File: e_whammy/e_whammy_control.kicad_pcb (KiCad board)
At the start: 4 copper layers, 17 x 30 mm, 17 parts, among them J1 I/O connector, U1 HT7550-1, U2 DRV5056, U3 TLV6001UIDBVR

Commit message: First shot at layout
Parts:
- removed C2: 10uF, Capacitor_SMD:C_0805_2012Metric
- removed R4: 10K, Resistor_SMD:R_0402_1005Metric
- removed REF**: hole_1.7mm, cycfi_library:hole_1.7mm
- removed U1: HT7550-1, Package_TO_SOT_SMD:SOT-89-3
- added C3: 10uF, Capacitor_SMD:C_0603_1608Metric, F.Cu at (137.5, 145.4)
- added C4: 10uF, Capacitor_SMD:C_0603_1608Metric, F.Cu at (140.2, 148.0)
- added D2: 1N4148WS, Diode_SMD:D_SOD-323, F.Cu at (137.0, 148.0)
- added D3: 1N4148WS, Diode_SMD:D_SOD-323, F.Cu at (147.4, 150.7)
- added D4: 1N4148WS, Diode_SMD:D_SOD-323, F.Cu at (154.4, 150.7)
- added D5: 1N4148WS, Diode_SMD:D_SOD-323, F.Cu at (157.9, 150.7)
- added G***: LOGO, cycfi_library:infinity_logo_4mm, F.Cu at (161.7, 151.3)
- added J2: Conn_01x03, cycfi_library:pin_header_1x3p_2.54mm_smd_horizontal, B.Cu at (154.8, 148.5)
- added J3: Conn_01x02, Connector_PinHeader_2.54mm:PinHeader_1x02_P2.54mm_Vertical, F.Cu at (146.9, 141.1)
- added J4: Conn_01x02, Connector_PinHeader_2.54mm:PinHeader_1x02_P2.54mm_Vertical, F.Cu at (157.4, 141.1)
- added R10: 10K, Resistor_SMD:R_0402_1005Metric, F.Cu at (147.4, 148.8)
- added R11: 10K, Resistor_SMD:R_0402_1005Metric, F.Cu at (157.4, 148.7)
- added R12: 10K, Resistor_SMD:R_0402_1005Metric, F.Cu at (157.4, 145.4)
- added R13: 10K, Resistor_SMD:R_0402_1005Metric, F.Cu at (157.4, 144.3)
- added R14: 10K, Resistor_SMD:R_0402_1005Metric, F.Cu at (161.3, 143.2)
- added R15: 10K, Resistor_SMD:R_0402_1005Metric, F.Cu at (142.7, 150.7)
- added R16: 10K, Resistor_SMD:R_0402_1005Metric, F.Cu at (143.8, 150.7)
- added R8: 100K, Resistor_SMD:R_0402_1005Metric, F.Cu at (166.1, 143.2)
- added R9: 100K, Resistor_SMD:R_0402_1005Metric, F.Cu at (166.1, 149.5)
- added RV3: 10K, cycfi_library:TC33X-2, F.Cu at (166.7, 146.3)
- C1: value 10uF -> 100nF; footprint Capacitor_SMD:C_0805_2012Metric -> Capacitor_SMD:C_0402_1005Metric
- D1: value 1N4148W -> 1N4148WS; footprint Diode_SMD:D_SOD-123 -> Diode_SMD:D_SOD-323
- J1: value I/O connector -> Conn_01x03; footprint Connector_PinHeader_2.54mm:PinHeader_1x03_P2.54mm_Vertical -> cycfi_library:pin_header_1x3p_2.54mm_smd_horizontal; moved to B.Cu
- R2: value 4.7K -> 10K
- R6: value 100K -> 47K
- RV1: value 5K -> 10K
- U2: value DRV5056 -> HT7550-1
- U3: value TLV6001UIDBVR -> TLV9004IPWR; footprint Package_TO_SOT_SMD:SOT-23-5 -> cycfi_library:TSSOP-14_4.4x5mm_P0.65mm
- moved R7 59.5 mm to (157.4, 146.5), turned to 0 degrees
- moved R5 53.9 mm to (157.4, 147.6), turned to 180 degrees
- moved U3 52.4 mm to (152.4, 146.4), turned to 0 degrees
- moved J1 49.8 mm to (149.2, 143.5), turned to 180 degrees
- moved D1 49.5 mm to (150.8, 150.7), turned to 0 degrees
- moved R2 47.3 mm to (147.9, 144.7)
- moved C1 47.3 mm to (144.9, 150.7)
- moved RV2 47.1 mm to (161.8, 146.3), turned to 0 degrees
- moved R3 46.5 mm to (147.4, 147.7), turned to 0 degrees
- moved R1 45.2 mm to (146.8, 144.7)
- moved R6 44.0 mm to (147.4, 146.4)
- moved RV1 42.3 mm to (144.2, 146.3), turned to 0 degrees
- moved U2 40.2 mm to (140.2, 145.4), turned to 0 degrees
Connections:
- C1 pad 1: Net-(D1-K) -> /VREF
- D1 pad 2: V+ -> /PR
- J1 pad 1: OUT -> HE_SENSOR
- R1 pad 2: Net-(R1-Pad2) -> Net-(U3A--)
- R2 pad 1: Net-(R2-Pad1) -> Net-(U3A--)
- R2 pad 2: 5v -> /PRE
- R3 pad 1: Net-(U2-OUT) -> /PRE
- R3 pad 2: Net-(U3-+) -> Net-(D3-K)
- R5 pad 1: Net-(U3-+) -> /PRE
- R5 pad 2: 5v -> Net-(D5-A)
- R6 pad 1: Net-(U3--) -> Net-(R6-Pad1)
- R6 pad 2: Net-(R6-Pad2) -> HE_SENSOR
- R7 pad 1: Net-(R7-Pad1) -> /RO2
- RV1 pad 1: Net-(R2-Pad1) -> GND
- RV1 pad 2: Net-(R4-Pad1) -> Net-(R6-Pad1)
- RV1 pad 3: Net-(R1-Pad2) -> 5v
- RV2 pad 1: Net-(R6-Pad2) -> /RO1
- RV2 pad 2: Net-(R7-Pad1) -> /RO1
- RV2 pad 3: Net-(R7-Pad1) -> /RO2
- U2 pad 1: 5v -> GND
- U2 pad 2: Net-(U2-OUT) -> Net-(D2-K)
- U2 pad 3: GND -> 5v
- U3 pad 1: Net-(U3-+) -> /PRE
- U3 pad 2: GND -> Net-(U3A--)
- U3 pad 3: Net-(U3--) -> HE_SENSOR
- U3 pad 4: Net-(R7-Pad1) -> 5v
- U3 pad 5: 5v -> /DHI
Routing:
- net Net-(R7-Pad1): track 21.5 -> 0.00 mm, vias 2 -> 0
- net 5v: track 9.59 -> 0.00 mm, vias 6 -> 0
- net Net-(U3--): track 8.92 -> 0.00 mm, vias 2 -> 0
- net Net-(D1-K): track 6.79 -> 0.00 mm
- net Net-(R4-Pad1): track 6.50 -> 0.00 mm, vias 2 -> 0
- net V+: track 6.42 -> 0.00 mm
- net Net-(R6-Pad2): track 6.17 -> 0.00 mm
- net Net-(R1-Pad2): track 4.40 -> 0.00 mm
- net OUT: track 3.34 -> 0.00 mm
- net Net-(U3-+): track 3.33 -> 0.00 mm
- net Net-(U2-OUT): track 2.90 -> 0.00 mm
- net Net-(R2-Pad1): track 1.40 -> 0.00 mm
- removed copper zone on In1.Cu, net 5v
- removed copper zone on B.Cu, net GND
- removed copper zone on F.Cu, net GND
- removed copper zone on In2.Cu, net GND
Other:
- board size 17 x 30 mm -> 34 x 14 mm
- copper layers 4 -> 2
- board text added: "CENTER"
- board text added: "DBO"
- board text added: "DEADBAND"
- board text added: "HE v1.0"
- board text added: "HE-SENSOR"
- board text added: "OUTPUT"
- board text added: "RANGE"
- board text added: "RGO"
- board text removed: "GAIN"
- board text removed: "OFFS"

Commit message: E-Whammy layout complete (first shot)
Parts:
- moved D2 2.73 mm to (139.5, 149.1), turned to 0 degrees
- moved J1 2.54 mm to (149.2, 146.0)
- moved J2 2.54 mm to (154.8, 146.0)
- moved U2 2.40 mm to (140.3, 143.1)
- moved C4 1.58 mm to (140.3, 146.4), turned to -90 degrees
- moved C3 1.51 mm to (138.7, 146.4), turned to -90 degrees
- moved R6 0.27 mm to (147.3, 146.2)
- moved R12 0.25 mm to (157.4, 145.2)
- moved R11 0.20 mm to (157.4, 148.9)
- moved R13 0.20 mm to (157.4, 144.1)
- moved R10 0.16 mm to (147.4, 149.0)
- moved R3 0.16 mm to (147.4, 147.9)
- moved RV1 0.14 mm to (144.1, 146.3)
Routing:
- net 5v: track 0.00 -> 44.8 mm, vias 0 -> 2
- net /DHI: track 0.00 -> 37.9 mm
- net /DLO: track 0.00 -> 32.8 mm
- net /PRE: track 0.00 -> 30.3 mm, vias 0 -> 3
- net V+: track 0.00 -> 20.6 mm, vias 0 -> 1
- net /VREF: track 0.00 -> 20.1 mm, vias 0 -> 2
- net /PR: track 0.00 -> 20.1 mm, vias 0 -> 2
- net /RO2: track 0.00 -> 19.4 mm
- net /NR: track 0.00 -> 13.9 mm, vias 0 -> 2
- net /RO1: track 0.00 -> 10.6 mm
- net GND: track 0.00 -> 9.81 mm, vias 0 -> 7
- net Net-(U3D--): track 0.00 -> 8.29 mm, vias 0 -> 2
- net Net-(D5-A): track 0.00 -> 7.05 mm
- net HE_SENSOR: track 0.00 -> 6.33 mm, vias 0 -> 1
- net Net-(D2-K): track 0.00 -> 5.98 mm
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- added copper zone on B.Cu, net GND
- added copper zone on F.Cu, net GND

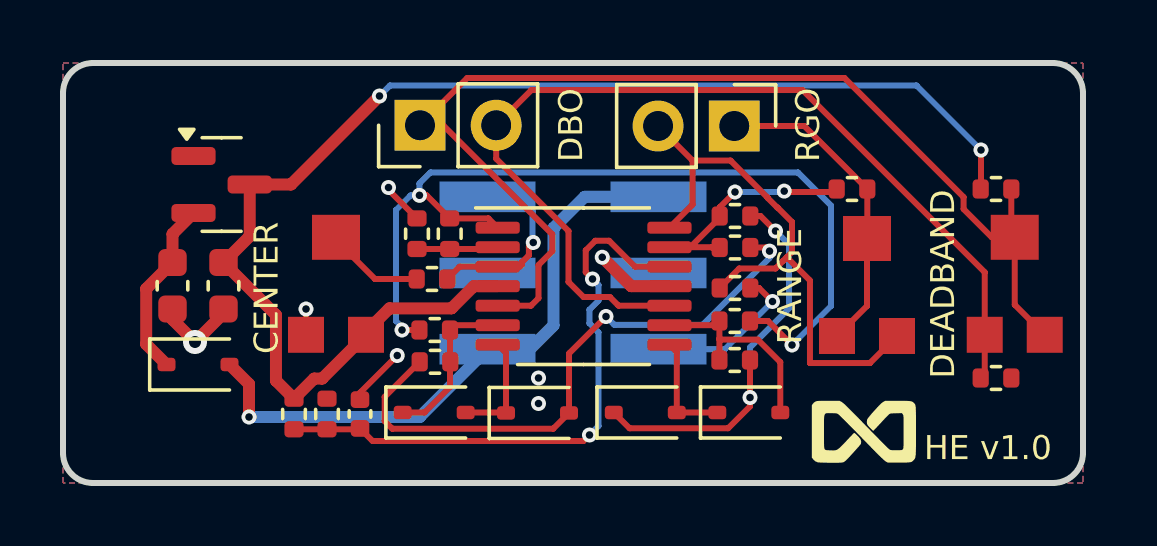
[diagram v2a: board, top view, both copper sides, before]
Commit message: E-Whammy layout looking good!
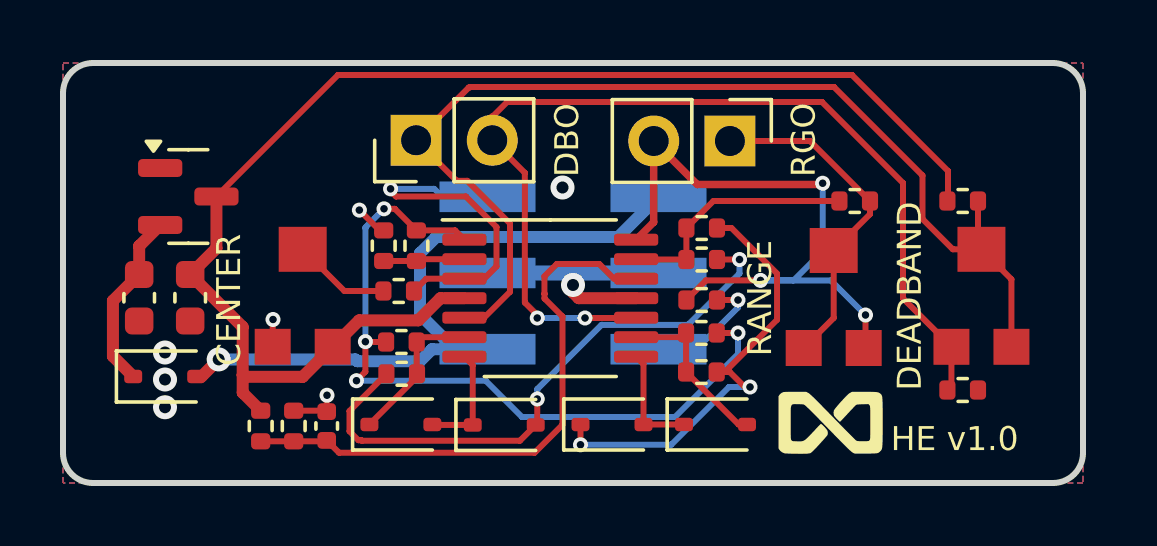
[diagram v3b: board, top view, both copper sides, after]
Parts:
- moved C1 1.18 mm to (143.8, 151.1)
- moved D3 1.18 mm to (146.3, 151.1)
- moved D5 1.18 mm to (156.8, 151.1)
- moved R1 1.18 mm to (145.7, 145.1)
- moved R10 1.18 mm to (146.3, 149.4)
- moved R12 1.18 mm to (156.3, 145.6)
- moved R13 1.18 mm to (156.3, 144.5)
- moved R16 1.18 mm to (142.7, 151.1)
- moved R6 1.18 mm to (146.2, 146.6)
- moved R7 1.18 mm to (156.3, 146.9)
- moved C3 1.18 mm to (137.5, 146.8)
- moved D2 1.18 mm to (138.4, 149.4)
- moved RV2 1.18 mm to (160.7, 146.7)
- moved D1 1.18 mm to (149.7, 151.1)
- moved D4 1.18 mm to (153.3, 151.1)
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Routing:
- net HE_SENSOR: track 6.33 -> 11.9 mm
- net /PRE: track 30.3 -> 25.4 mm, vias 3 -> 4
- net V+: track 20.6 -> 23.6 mm
- net /RO2: track 19.4 -> 22.4 mm, vias 0 -> 3
- net GND: track 9.81 -> 11.8 mm, vias 7 -> 8
- net /DHI: track 37.9 -> 36.4 mm
- net /NR: track 13.9 -> 15.3 mm
- net Net-(D5-A): track 7.05 -> 5.78 mm
- net /VREF: track 20.1 -> 19.3 mm, vias 2 -> 0
- net /RO1: track 10.6 -> 11.3 mm
- net 5v: track 44.8 -> 45.4 mm, vias 2 -> 0
- net /DLO: track 32.8 -> 33.3 mm, vias 0 -> 2
- net Net-(U3D--): track 8.29 -> 8.20 mm, vias 2 -> 0

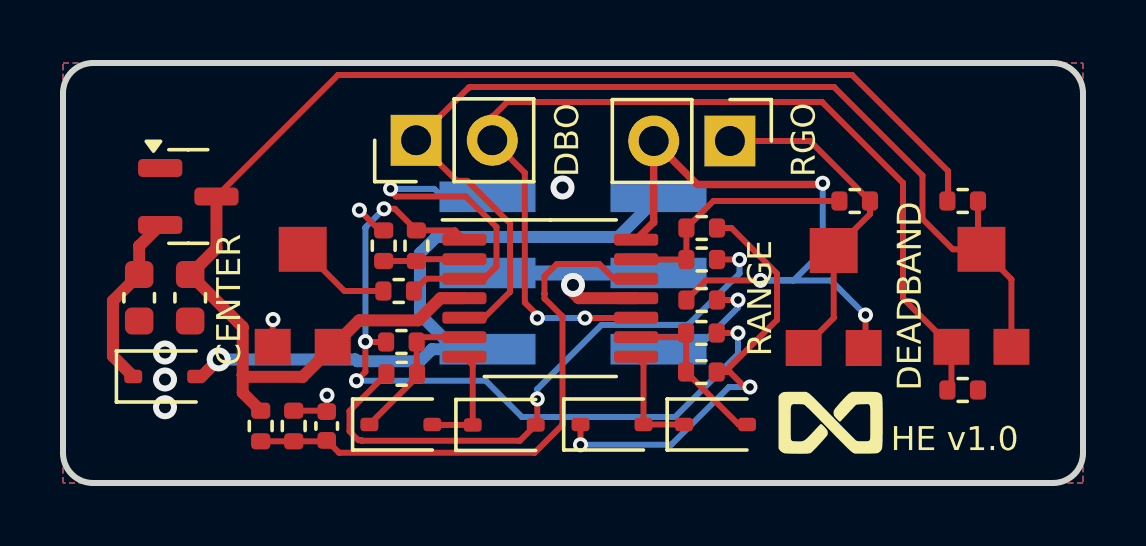
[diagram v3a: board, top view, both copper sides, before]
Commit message: Added bridged jumper pads for overriding the pots
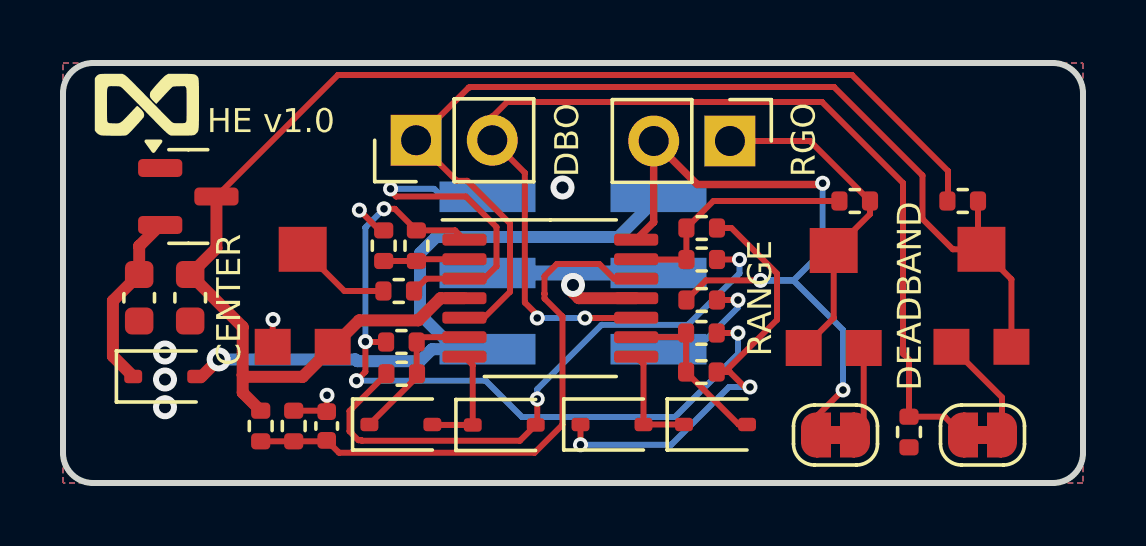
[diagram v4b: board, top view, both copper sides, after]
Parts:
- added JP1: SolderJumper_2_Bridged, Jumper:SolderJumper-2_P1.3mm_Bridged_RoundedPad1.0x1.5mm, F.Cu at (165.7, 151.4)
- added JP2: SolderJumper_2_Bridged, Jumper:SolderJumper-2_P1.3mm_Bridged_RoundedPad1.0x1.5mm, F.Cu at (160.8, 151.4)
- moved G*** 25.1 mm to (137.8, 140.4)
- moved R9 2.27 mm to (163.2, 151.3), turned to 90 degrees
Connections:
- RV2 pad 3: /RO2 -> Net-(JP2-B)
- RV3 pad 1: /DLO -> Net-(JP1-B)
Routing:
- net Net-(JP1-B): track 0.00 -> 3.64 mm
- net Net-(JP2-B): track 0.00 -> 3.10 mm
- net /DLO: track 33.3 -> 35.6 mm
- net /RO2: track 22.4 -> 24.6 mm

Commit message: More refinements
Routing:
- net GND: vias 8 -> 11
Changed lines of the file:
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@@
 			)
 		)
-		(property "Description" ""
+		(property "Description" "Resistor"
 			(at 0 0 90)
 			(layer "F.Fab")
@@
 			)
 		)
-		(property "Description" ""
+		(property "Description" "Resistor"
 			(at 0 0 0)
 			(layer "F.Fab")
@@
 			)
 		)
-		(property "Description" ""
+		(property "Description" "Resistor"
 			(at 0 0 0)
 			(layer "F.Fab")
@@
 			)
 		)
-		(property "Description" ""
+		(property "Description" "Resistor"
 			(at 0 0 90)
 			(layer "F.Fab")
@@
 			)
 		)
-		(property "Description" ""
+		(property "Description" "Resistor"
 			(at 0 0 0)
 			(layer "F.Fab")
@@
 			)
 		)
-		(property "Description" ""
+		(property "Description" "Resistor"
 			(at 0 0 0)
 			(layer "F.Fab")
@@
 			)
 		)
-		(property "Description" ""
+		(property "Description" "Trim-potentiometer"
 			(at 0 0 0)
 			(layer "F.Fab")
@@
 			)
 		)
-		(property "Description" ""
+		(property "Description" "Trim-potentiometer"
 			(at 0 0 0)
 			(layer "F.Fab")
@@
 			)
 		)
-		(property "Description" ""
+		(property "Description" "Resistor"
 			(at 0 0 0)
 			(layer "F.Fab")
@@
 			)
 		)
-		(property "Description" ""
+		(property "Description" "Resistor"
 			(at 0 0 90)
 			(layer "F.Fab")
@@
 			)
 		)
-		(property "Description" ""
+		(property "Description" "Resistor"
 			(at 0 0 90)
 			(layer "F.Fab")
@@
 			)
 		)
-		(property "Description" ""
+		(property "Description" "Resistor"
 			(at 0 0 90)
 			(layer "F.Fab")
@@
 			)
 		)
-		(property "Description" ""
+		(property "Description" "Resistor"
 			(at 0 0 0)
 			(layer "F.Fab")
@@
 			)
 		)
-		(property "Description" ""
+		(property "Description" "Resistor"
 			(at 0 0 0)
 			(layer "F.Fab")
@@
 			)
 		)
-		(property "Description" ""
+		(property "Description" "Resistor"
 			(at 0 0 0)
 			(layer "F.Fab")
@@
 			)
 		)
-		(property "Description" ""
+		(property "Description" "Trim-potentiometer"
 			(at 0 0 0)
 			(layer "F.Fab")
@@
 			)
 		)
-		(property "Description" ""
+		(property "Description" "Resistor"
 			(at 0 0 0)
 			(layer "F.Fab")
@@
 			)
 		)
-		(property "Description" ""
+		(property "Description" "Resistor"
 			(at 0 0 0)
 			(layer "F.Fab")
@@
 	)
 	(via
+		(at 161.7 147.225)
+		(size 0.5)
+		(drill 0.25)
+		(layers "F.Cu" "B.Cu")
+		(net 2)
+	)
+	(via
+		(at 164.625 147.25)
+		(size 0.5)
+		(drill 0.25)
+		(layers "F.Cu" "B.Cu")
+		(net 2)
+	)
+	(via
 		(at 151.65 143.15)
 		(size 0.8)
@@
 	)
 	(via
+		(at 158.35 144.375)
+		(size 0.5)
+		(drill 0.25)
+		(layers "F.Cu" "B.Cu")
+		(net 2)
+	)
+	(via
 		(at 143.8 150.075)
 		(size 0.5)
@@
 	)
 	(segment
-		(start 149.805 140.3)
-		(end 149.31 140.795)
+		(start 160.3 140.3)
+		(end 149.805 140.3)
 		(width 0.2)
 		(layer "F.Cu")
@@
 	)
 	(segment
-		(start 154.095 147.5)
-		(end 154.105 147.49)
+		(start 163 143)
+		(end 160.3 140.3)
 		(width 0.2)
 		(layer "F.Cu")
@@
 	)
 	(segment
-		(start 149.31 141.575)
-		(end 149.31 140.795)
-		(width 0.25)
-		(layer "F.Cu")
-		(net 15)
-	)
-	(segment
-		(start 150.395606 143.840606)
-		(end 150.395606 146.987106)
+		(start 154.095 147.5)
+		(end 154.105 147.49)
 		(width 0.2)
 		(layer "F.Cu")
@@
 	)
 	(segment
-		(start 163 148.689999)
+		(start 163 150.59)
 		(end 163 143)
 		(width 0.2)
@@
 	)
 	(segment
-		(start 150.395606 142.660606)
-		(end 149.31 141.575)
-		(width 0.2)
+		(start 149.31 141.575)
+		(end 149.31 140.795)
+		(width 0.25)
 		(layer "F.Cu")
 		(net 15)
 	)
 	(segment
-		(start 163.2 150.79)
-		(end 163.2 148.889999)
+		(start 150.395606 143.840606)
+		(end 150.395606 146.987106)
 		(width 0.2)
 		(layer "F.Cu")
@@
 	)
 	(segment
-		(start 152.4 147.5)
-		(end 154.095 147.5)
+		(start 149.805 140.3)
+		(end 149.31 140.795)
 		(width 0.2)
 		(layer "F.Cu")
@@
 	)
 	(segment
-		(start 163.2 148.889999)
-		(end 163 148.689999)
+		(start 150.395606 142.660606)
+		(end 149.31 141.575)
 		(width 0.2)
 		(layer "F.Cu")
@@
 	)
 	(segment
-		(start 163 143)
-		(end 160.3 140.3)
+		(start 152.4 147.5)
+		(end 154.095 147.5)
 		(width 0.2)
 		(layer "F.Cu")
@@
 	)
 	(segment
-		(start 160.3 140.3)
-		(end 149.805 140.3)
+		(start 163.2 150.79)
+		(end 163 150.59)
 		(width 0.2)
 		(layer "F.Cu")

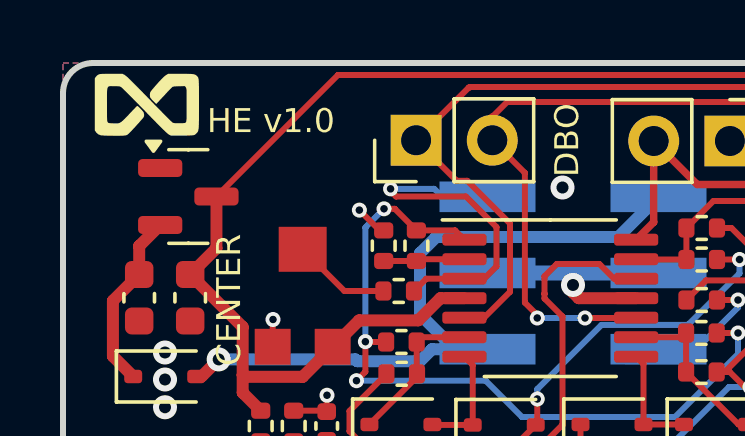
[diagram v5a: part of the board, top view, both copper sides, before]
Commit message: Updated circuit matching the E-Whammy control design.
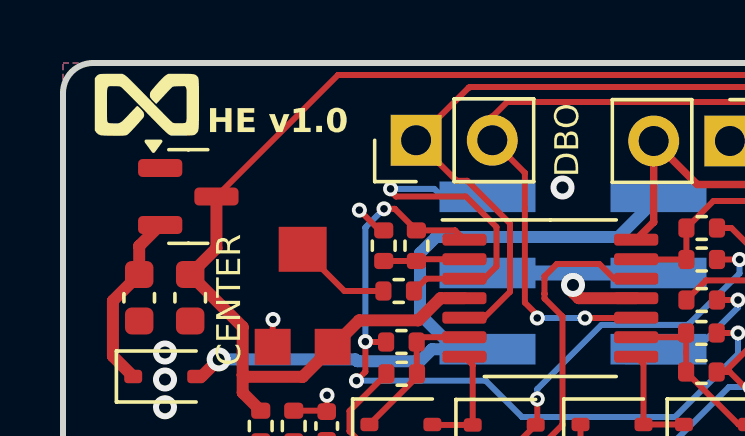
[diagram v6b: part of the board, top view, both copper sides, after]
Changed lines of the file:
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@@
 			(font
 				(size 0.8 0.8)
-				(thickness 0.1)
+				(thickness 0.15)
+				(bold yes)
 			)
 			(justify left bottom)

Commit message: Recover lost refinements
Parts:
- moved R14 1.47 mm to (161.8, 142.2)
- moved R8 1.42 mm to (165.0, 142.2)
- moved C4 1.10 mm to (138.6, 147.7)
- moved U2 1.10 mm to (138.5, 144.3)
- moved C3 1.10 mm to (136.9, 147.7)
- moved D2 1.10 mm to (137.7, 150.3)
- moved G*** 0.61 mm to (137.6, 141.0)
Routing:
- net /DHI: track 36.4 -> 38.7 mm
- net /RO1: track 11.3 -> 12.7 mm
- net Net-(U3D--): track 8.20 -> 9.56 mm
- net V+: track 23.6 -> 24.7 mm
- net /DLO: track 35.6 -> 36.6 mm
- net 5v: track 45.4 -> 46.0 mm
- net GND: vias 11 -> 14
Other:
- board text added: "DBAND"
- board text removed: "DEADBAND"
